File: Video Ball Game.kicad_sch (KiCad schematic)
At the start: 147 parts, among them J1 RIGHT CONTROL, J10 GND, J11 GND, J12 D, J13 BL, J14 CL, J15 Video, J16 BR, J2 LEFT CONTROL, J3 FS, J4 UL, J5 NH, J6 LL, J7 GND, J8 LS, J9 GND, U1 4011, U10 4011, U11 4001, U12 4001, U13 4001, U2 4011, U3 4011, U4 4011, U5 4001, U6 4001, U7 4001, U8 4001, U9 4011

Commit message: jon's changes
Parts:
- removed R53, R54: 10M, Resistor_THT:R_Axial_DIN0204_L3.6mm_D1.6mm_P5.08mm_Horizontal, symbol Device:R
- removed S3: Power, Connector_PinHeader_2.54mm:PinHeader_1x03_P2.54mm_Vertical, symbol Switch:SW_DPST
- added C35, C36, C37, C38, C39, C40, C41, C42, C43, C44, C45, C46, C47: 0.1uF, Capacitor_THT:C_Disc_D3.0mm_W1.6mm_P2.50mm, symbol Device:C
- added R? (x2): 10k, Resistor_THT:R_Axial_DIN0204_L3.6mm_D1.6mm_P5.08mm_Horizontal, symbol Device:R
- added S?: Power, Connector_PinHeader_2.54mm:PinHeader_1x03_P2.54mm_Vertical, symbol Switch:SW_DPST
- added U14: L7806, Connector_PinSocket_2.54mm:PinSocket_1x03_P2.54mm_Vertical, symbol Regulator_Linear:L7806
- C30: value 2200 16VW -> 0.33uF -2.2uF (Jon 470uF); footprint Capacitor_THT:CP_Radial_D18.0mm_P7.50mm -> Capacitor_THT:C_Disc_D3.8mm_W2.6mm_P2.50mm
- C31: value 22 16VW -> 22uF-100uF 16VW. Dave showed this even works with 0.5uF @17:10 on #1085
- U5: symbol 4xxx:4011 -> 4xxx:4001
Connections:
- net Earth: now also C35.2, C36.2, C37.2, C38.2, C39.2, C40.2, C41.2, C42.2, C43.2, C44.2, C45.2, C46.2, C47.2, U14.2 (GND)
- net G: now also U5.5, R?.1; no longer RV3.3, U5.10, U5.13
- net H: now also U5.2; no longer J12.1 (Pin_1), U5.11, U5.9
- net at C30.1: now also S?.2, S?.4
- net at D7.2 (A), D8.1 (K), R42.1: now also TR1.3 (E), TR2.3 (E)
- net at C11.1, D12.2 (A), R25.2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: no longer U5.2
- net at C12.1, D11.2 (A), R26.2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: no longer U5.5
- net at BT1.1 (+): now also S?.1
- net +9V renamed +6V
- net +6V: now also C35.1, C36.1, C37.1, C38.1, C39.1, C40.1, C41.1, C42.1, C43.1, C44.1, C45.1, C46.1, C47.1, R?.2, R?.2, U14.3 (OUT)
- new net: J12.1 (Pin_1), U5.11, U5.9
- new net: S?.3, U14.1 (IN)
- new net BX: RV3.3, U5.10, U5.13
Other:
- note added: "6V Regulator"
- note added: "Ball X (Horiz) position SR latch BX low=right --> BX high= left <--"
- note added: "Ball X (Horiz) position is voltage across C27"
- note added: "Ball Y (vertical) position Voltage at pins 8 and 9 decrease as the ball is falling."
- note added: "Decoupling capacitors EEVBlog#1085@12:10. Dave used 100nF Film caps."
- note added: "Inject bat motion onto ball Y at moment of impact"
- note added: "Left bat frame pulse"
- note added: "POWER"
- note added: "Right bat frame pulse"
- note added: "Video Ball Game, Electronics Australia May 1976"
- note removed: "Flip-flip low=right --> high= left <--"
- note removed: "Trans gets velocity at moment of impact"
- note removed: "edge squaring"
- note removed: "horizontal position of ball"
- note removed: "low supply impedance. Always on!!! leakage??"
- note removed: "vertical velocity of ball. V (pin8&9) falls as the ball is falling."
- moved on the sheet: BT1, C31, H1, H2, H3, H4

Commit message: fixed all footprints - pcb need retracing.
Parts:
- C1, C21, C28, C29, C32: value .01 -> 10nF red; footprint Capacitor_THT:C_Disc_D3.0mm_W1.6mm_P2.50mm -> Capacitor_THT:C_Rect_L7.2mm_W3.0mm_P5.00mm_FKS2_FKP2_MKS2_MKP2
- C10, C19, C3, C4, C9: value .01 -> 10nF red
- C11, C12: value .0047 -> 4.7nF red
- C13, C14, C18: value 100pF -> 100pF blue; footprint Capacitor_THT:C_Axial_L3.8mm_D2.6mm_P7.50mm_Horizontal -> Capacitor_THT:C_Disc_D3.0mm_W1.6mm_P2.50mm
- C15, C16, C33: value 0.1 -> 100nF red; footprint Capacitor_THT:C_Disc_D3.0mm_W1.6mm_P2.50mm -> Capacitor_THT:C_Rect_L7.2mm_W3.0mm_P5.00mm_FKS2_FKP2_MKS2_MKP2
- C17, C22: value 0.033 -> 33nF red; footprint Capacitor_THT:C_Disc_D3.0mm_W1.6mm_P2.50mm -> Capacitor_THT:C_Rect_L7.2mm_W3.0mm_P5.00mm_FKS2_FKP2_MKS2_MKP2
- C2, C5, C7, C8: value 330pF -> 330pF blue; footprint Capacitor_THT:C_Axial_L3.8mm_D2.6mm_P7.50mm_Horizontal -> Capacitor_THT:C_Disc_D5.1mm_W3.2mm_P5.00mm
- C20: value 220pF -> 220pF blue; footprint Capacitor_THT:C_Rect_L7.2mm_W3.0mm_P5.00mm_FKS2_FKP2_MKS2_MKP2 -> Capacitor_THT:C_Disc_D3.0mm_W1.6mm_P2.50mm
- C23: footprint Capacitor_THT:C_Disc_D3.8mm_W2.6mm_P2.50mm -> Capacitor_THT:CP_Radial_Tantal_D4.5mm_P5.00mm
- C24, C6: value 100pF -> 100pF blue
- C25, C26: value 330pF -> 330pF blue
- C27: value 220 16VW -> 220uF elec 16VW 8x11 mm P 3.5; footprint Capacitor_THT:CP_Radial_D8.0mm_P5.00mm -> Capacitor_THT:C_Radial_D8.0mm_H11.5mm_P3.50mm
- C30: value 0.33uF -2.2uF (Jon 470uF) -> 0.33uF elec -2.2uF (Jon 470uF)
- C31: value 22uF-100uF 16VW. Dave showed this even works with 0.5uF @17:10 on #1085 -> 22uF elec -100uF 16VW. Dave showed this even works with 0.5uF @17:10 on #1085
- C34: value 47 16VW -> 47uF elec 16VW radial 5x11mm P2.0; footprint Capacitor_THT:CP_Radial_D8.0mm_P5.00mm -> Capacitor_THT:C_Radial_D5.0mm_H11.0mm_P2.00mm
- C35, C36, C37, C38, C39, C40, C41, C42, C43, C44, C45, C46, C47: value 0.1uF -> 100nF bypass red; footprint Capacitor_THT:C_Disc_D3.0mm_W1.6mm_P2.50mm -> Capacitor_THT:C_Rect_L7.2mm_W5.5mm_P5.00mm_FKS2_FKP2_MKS2_MKP2
- D1, D10, D11, D12, D2, D3, D4, D5, D6, D7, D8, D9: value D -> 1N4148; footprint Diode_THT:D_A-405_P7.62mm_Horizontal -> Diode_THT:D_DO-35_SOD27_P7.62mm_Horizontal
- R1, R10, R11, R12, R13, R14, R15, R16, R17, R18, R19, R2, R20, R21, R22, R23, R24, R25, R26, R27, R28, R29, R3, R30, R31, R32, R33, R34, R35, R36, R37, R38, R39, R4, R40, R41, R43, R44, R45, R46, R47, R48, R49, R5, R50, R51, R52, R6, R7, R8, R9: footprint Resistor_THT:R_Axial_DIN0204_L3.6mm_D1.6mm_P5.08mm_Horizontal -> Resistor_THT:R_Axial_DIN0207_L6.3mm_D2.5mm_P10.16mm_Horizontal
- R42: value 470 -> 470k; footprint Resistor_THT:R_Axial_DIN0204_L3.6mm_D1.6mm_P5.08mm_Horizontal -> Resistor_THT:R_Axial_DIN0207_L6.3mm_D2.5mm_P10.16mm_Horizontal
- R53, R54: renamed from R?; footprint Resistor_THT:R_Axial_DIN0204_L3.6mm_D1.6mm_P5.08mm_Horizontal -> Resistor_THT:R_Axial_DIN0207_L6.3mm_D2.5mm_P10.16mm_Horizontal
- RV3: value 100k LIN SPEED -> 100k linear speed
- S7: value INTERACTION -> Interaction
- U1, U10, U2, U3, U4, U9: value 4011 -> 4011 QUAD NAND
- U11, U12, U13, U5, U6, U7, U8: value 4001 -> 4001 QUAD NOR
- U14: footprint Connector_PinSocket_2.54mm:PinSocket_1x03_P2.54mm_Vertical -> Package_TO_SOT_THT:TO-220-3_Vertical
- gave numbers to parts that had none: 1
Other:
- moved on the sheet: R50, R51, R54

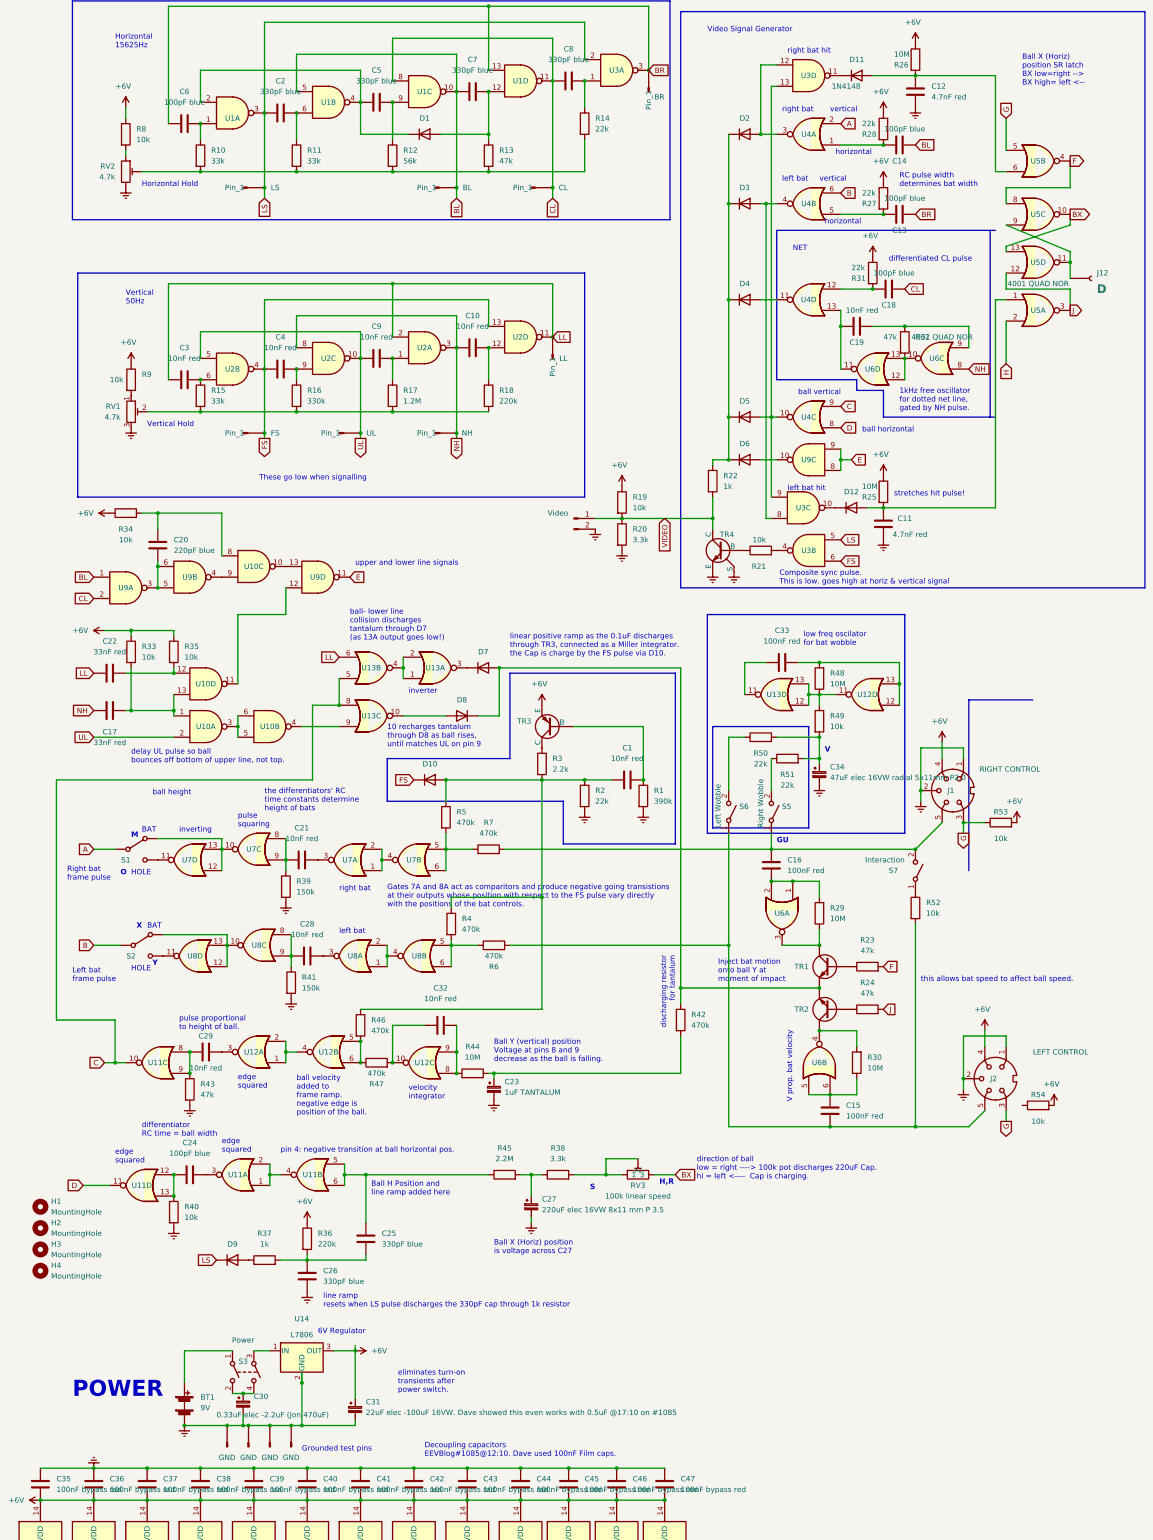
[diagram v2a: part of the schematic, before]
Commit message: USB power. removed all traces for retracing.
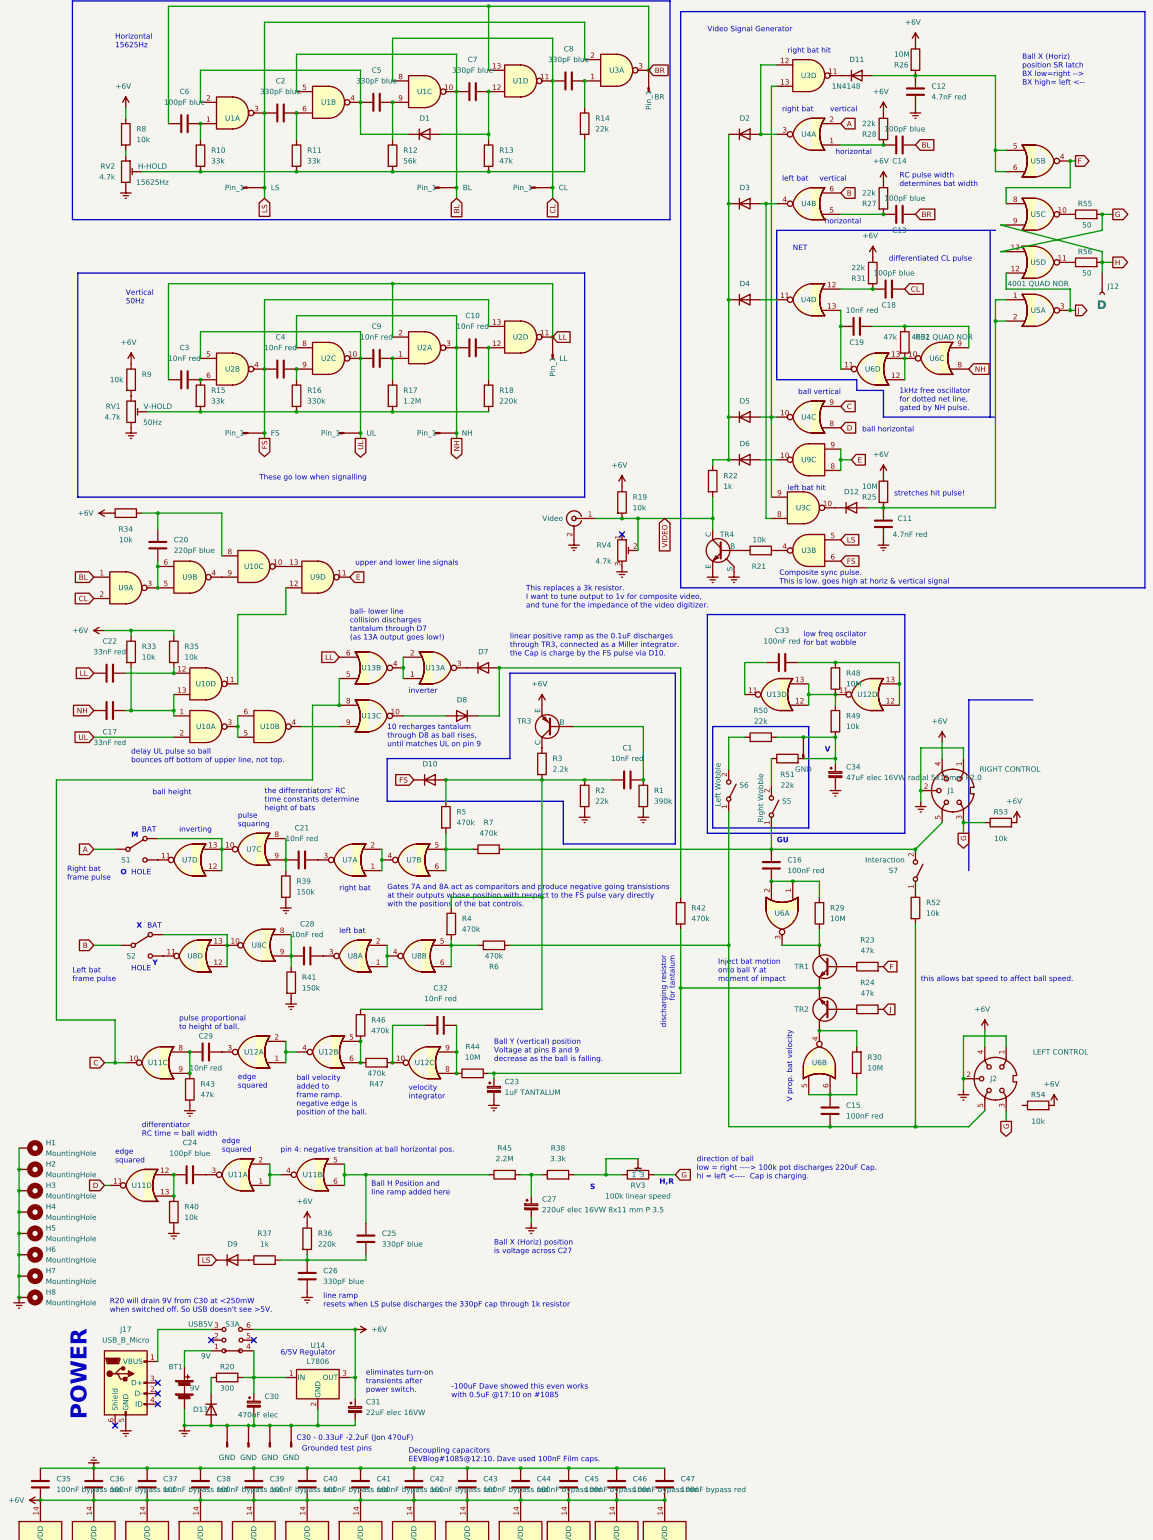
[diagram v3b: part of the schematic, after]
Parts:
- removed H2, H3, H4: MountingHole, MountingHole:MountingHole_2.2mm_M2_ISO14580_Pad_TopBottom, symbol Mechanical:MountingHole
- added D13: 1N4148, Diode_THT:D_DO-35_SOD27_P7.62mm_Horizontal, symbol Device:D
- added H2, H3, H4, H5, H6, H7, H8: MountingHole, MountingHole:MountingHole_2.5mm_Pad, symbol Mechanical:MountingHole_Pad
- added J17: USB_B_Micro, Connector_PinHeader_2.54mm:PinHeader_1x02_P2.54mm_Vertical, symbol Connector:USB_B_Micro
- added J?: GND, Connector_PinSocket_2.54mm:PinSocket_1x01_P2.54mm_Vertical, symbol Connector:Conn_01x01_Male
- added R55, R56: 50, Resistor_THT:R_Axial_DIN0207_L6.3mm_D2.5mm_P10.16mm_Horizontal, symbol Device:R
- added RV4: 4.7k, Potentiometer_THT:Potentiometer_Bourns_3266Y_Vertical, symbol Device:R_Potentiometer_Trim
- C30: value 0.33uF elec -2.2uF (Jon 470uF) -> 470uF elec; footprint Capacitor_THT:C_Disc_D3.8mm_W2.6mm_P2.50mm -> Capacitor_THT:CP_Radial_D10.0mm_P5.00mm
- C31: value 22uF elec -100uF 16VW. Dave showed this even works with 0.5uF @17:10 on #1085 -> 22uF elec 16VW
- H1: footprint MountingHole:MountingHole_2.2mm_M2_ISO14580_Pad_TopBottom -> MountingHole:MountingHole_2.5mm_Pad; symbol Mechanical:MountingHole -> Mechanical:MountingHole_Pad
- J15: footprint Connector_PinSocket_2.54mm:PinSocket_1x02_P2.54mm_Vertical -> Connector_PinHeader_2.54mm:PinHeader_1x02_P2.54mm_Vertical; symbol Connector:Conn_01x02_Male -> Connector:Conn_Coaxial
- R20: value 3.3k -> 300
- R50, R51, R52: footprint Resistor_THT:R_Axial_DIN0207_L6.3mm_D2.5mm_P10.16mm_Horizontal -> Library:no pads
- RV1: Field4 (none) -> 50Hz; Field5 (none) -> V-HOLD
- RV2: Field4 (none) -> 15625Hz; Field5 (none) -> H-HOLD
- RV3: footprint Potentiometer_THT:Potentiometer_Bourns_3266Y_Vertical -> Connector_PinHeader_2.54mm:PinHeader_1x03_P2.54mm_Vertical
- S3: value Power -> Power USB/9V; symbol Switch:SW_DPST -> SW_DP3T:SW_DP3T; Field4 (none) -> USB5V; Field5 (none) -> 9V
- S7: footprint Connector_PinSocket_2.54mm:PinSocket_1x02_P2.54mm_Vertical -> Connector_PinHeader_2.54mm:PinHeader_1x02_P2.54mm_Vertical
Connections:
- net +6V: now also S3.6
- net Earth: now also H1.1, D13.2 (A), H2.1, H3.1, H4.1, H5.1, H6.1, H7.1, H8.1, J17.5 (GND), RV4.3; no longer R20.2
- net G: now also RV3.3, U5.13, R55.2; no longer U5.5
- net H: now also J12.1 (Pin_1), U5.9, R56.2; no longer U5.2
- net VIDEO: now also RV4.2; no longer R20.1
- net at D7.2 (A), D8.1 (K), R42.1: no longer TR1.3 (E), TR2.3 (E)
- net at C23.1, R42.2, R44.2: now also TR1.3 (E), TR2.3 (E)
- net at C11.1, D12.2 (A), R25.2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: now also U5.2
- net at C30.1, S3.4: now also R20.2, U14.1 (IN); no longer S3.2
- net at C12.1, D11.2 (A), R26.2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: now also U5.5
- net at C34.1, R49.2, R50.2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: now also J?.1 (Pin_1)
- net at S3.3: now also J17.1 (VBUS); no longer U14.1 (IN)
- removed net BX: RV3.3, U5.10, U5.13
- new net: R55.1, U5.10
- new net: D13.1 (K), R20.1
- new net: R56.1, U5.11
- no-connect marks 0 -> 7
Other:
- note added: "-100uF Dave showed this even works with 0.5uF @17:10 on #1085"
- note added: "6/5V Regulator"
- note added: "C30 - 0.33uF -2.2uF (Jon 470uF)"
- note added: "R20 will drain 9V from C30 at <250mW when switched off. So USB doesn't see >5V."
- note added: "This replaces a 3k resistor. I want to tune output to 1v for composite video, and tune for the impedance of the video digitizer."
- note removed: "6V Regulator"
- note removed: "Horizontal Hold"
- note removed: "Vertical Hold"
- moved on the sheet: BT1, C30, C34, J12, R42, R48, R49, S5, S6, U14
